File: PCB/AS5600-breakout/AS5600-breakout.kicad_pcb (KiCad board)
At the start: 2 copper layers, 1 part, among them U1 AS5600

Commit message: initial PCB for encoder
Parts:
- added C1: 100nF, Capacitor_THT:CP_Radial_D6.3mm_P2.50mm, F.Cu at (87.1, 99.6)
- added C2: 1uF, Capacitor_THT:CP_Radial_D8.0mm_P3.50mm, F.Cu at (75.1, 100.5)
- added J1: Conn_01x02, Connector_PinHeader_2.54mm:PinHeader_1x02_P2.54mm_Vertical, F.Cu at (93.6, 100.7)
- added J2: Conn_01x02, Connector_PinHeader_2.54mm:PinHeader_1x02_P2.54mm_Vertical, F.Cu at (97.2, 100.7)
- added J3: Conn_01x05_Female, Connector_PinHeader_2.54mm:PinHeader_1x05_P2.54mm_Horizontal, F.Cu at (111.8, 86.4)
- added J4: Conn_01x03_Male, Connector_PinHeader_2.54mm:PinHeader_1x03_P2.54mm_Vertical, F.Cu at (83.0, 98.0)
- added R1: 4.7k, Resistor_THT:R_Axial_DIN0207_L6.3mm_D2.5mm_P7.62mm_Horizontal, F.Cu at (100.3, 80.0)
- added R2: 4.7k, Resistor_THT:R_Axial_DIN0207_L6.3mm_D2.5mm_P7.62mm_Horizontal, F.Cu at (73.9, 93.4)
- moved U1 10.5 mm to (83.8, 85.1)
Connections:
- U1 pad 1: Net-(U1-Pad1) -> +5V
- U1 pad 3: Net-(U1-Pad3) -> OUT
- U1 pad 4: Net-(U1-Pad4) -> GND
- U1 pad 6: Net-(U1-Pad6) -> SDA
- U1 pad 7: Net-(U1-Pad7) -> SCL
- U1 pad 8: Net-(U1-Pad8) -> DIR

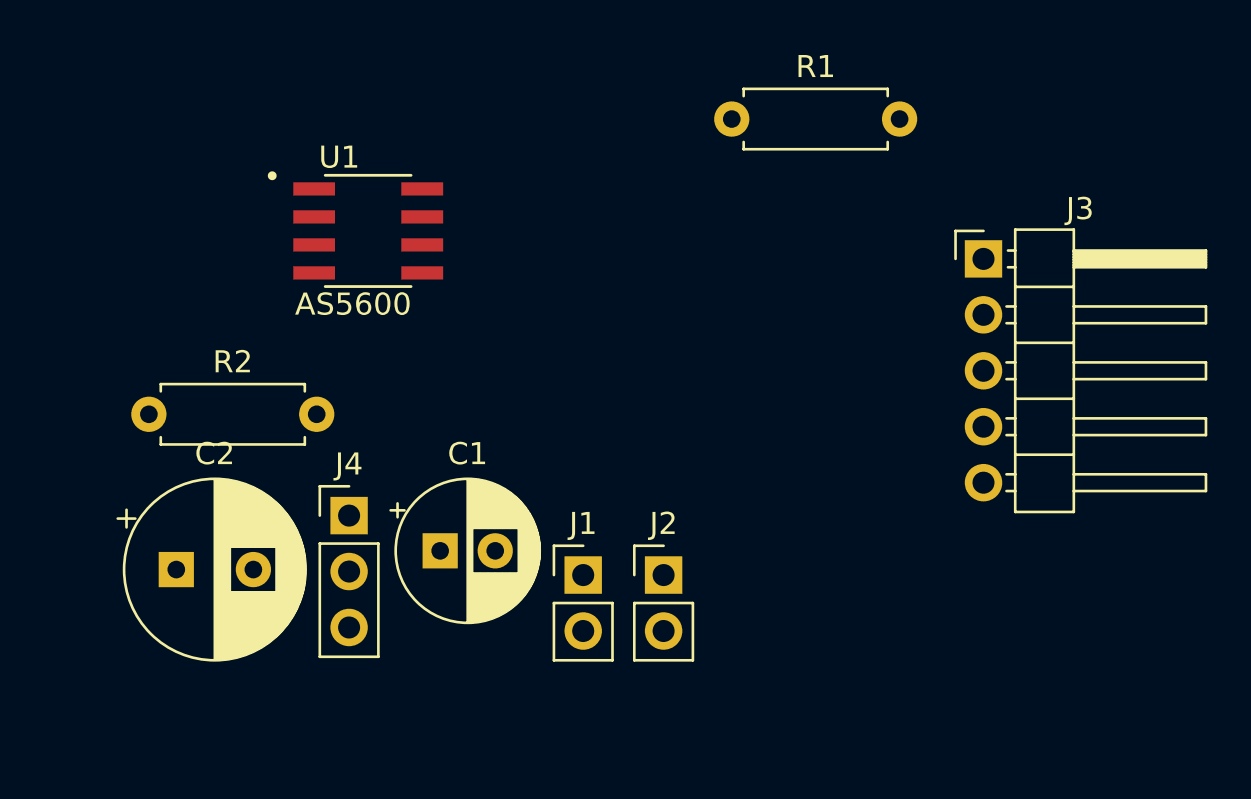
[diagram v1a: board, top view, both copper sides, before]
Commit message: first pcb has been cut for encoders, looks good!
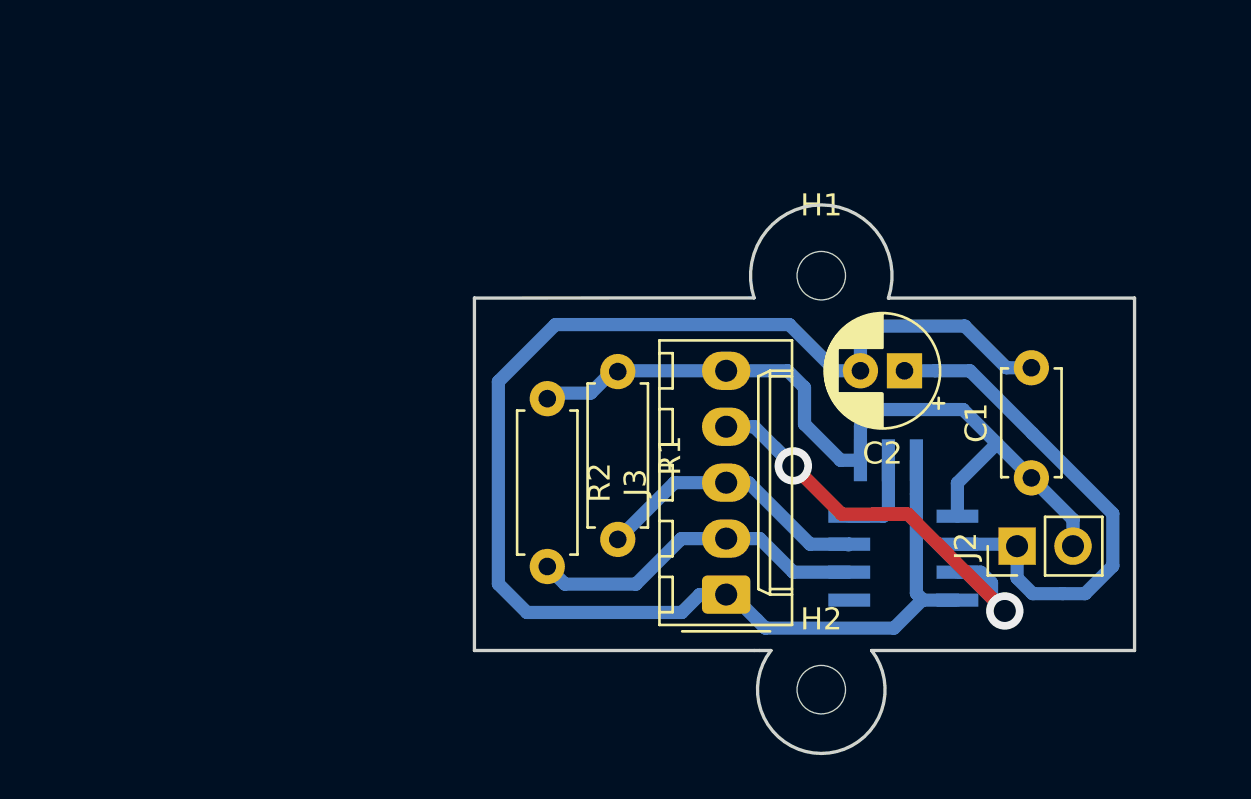
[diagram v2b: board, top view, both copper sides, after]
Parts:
- removed J1: Conn_01x02, Connector_PinHeader_2.54mm:PinHeader_1x02_P2.54mm_Vertical
- added H1: MountingHole, AS5600-breakout:MountingHole_2.2mm_M2_small, F.Cu at (104.4, 87.1)
- added H2: MountingHole, AS5600-breakout:MountingHole_2.2mm_M2_small, F.Cu at (104.4, 105.9)
- C1: footprint Capacitor_THT:CP_Radial_D6.3mm_P2.50mm -> Capacitor_THT:C_Disc_D4.7mm_W2.5mm_P5.00mm
- C2: footprint Capacitor_THT:CP_Radial_D8.0mm_P3.50mm -> Capacitor_THT:CP_Radial_D5.0mm_P2.00mm
- J3: footprint Connector_PinHeader_2.54mm:PinHeader_1x05_P2.54mm_Horizontal -> Connector_Molex:Molex_KK-254_AE-6410-05A_1x05_P2.54mm_Vertical
- J4: footprint Connector_PinHeader_2.54mm:PinHeader_1x03_P2.54mm_Vertical -> AS5600-breakout:SOIC127_solder_switch; moved to B.Cu
- U1: moved to B.Cu
- moved C2 34.3 mm to (108.2, 91.4), turned to 180 degrees
- moved U1 28.5 mm to (108.1, 99.9), turned to 180 degrees
- moved C1 27.0 mm to (113.9, 96.3), turned to 90 degrees
- moved J4 24.4 mm to (106.8, 93.0), turned to 90 degrees
- moved J3 19.2 mm to (100.1, 101.6), turned to 90 degrees
- moved R2 18.1 mm to (92.0, 92.7), turned to 270 degrees
- moved J2 16.1 mm to (113.3, 99.4), turned to 90 degrees
- moved R1 12.6 mm to (95.2, 91.5), turned to 270 degrees
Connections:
- J3 pad 1: +5V -> GND
- J3 pad 5: GND -> +5V
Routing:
- net GND: track 0.00 -> 66.7 mm
- net +5V: track 0.00 -> 36.2 mm
- net Net-(C2-Pad1): track 0.00 -> 23.9 mm
- net OUT: track 0.00 -> 22.2 mm, vias 0 -> 2
- net SDA: track 0.00 -> 15.3 mm
- net SCL: track 0.00 -> 12.5 mm
- net DIR: track 0.00 -> 4.18 mm
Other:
- board outline added: 30 x 24.9 mm
- net class Default: clearance 0.2 -> 0.3; trace_width 0.25 -> 0.6; via_dia 0.8 -> 1.7; via_drill 0.4 -> 0.8
- rule trace_clearance: 0.2 -> 0.3
- rule trace_min: 0.2 -> 0.5
